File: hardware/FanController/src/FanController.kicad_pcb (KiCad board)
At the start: 2 copper layers, 54 x 12 mm, 12 parts, among them J1 MC 1,5/2, J2 Fan, J3 Fan, J4 Fan, J5 Fan, U1 12F1501, U2 MCP9701A

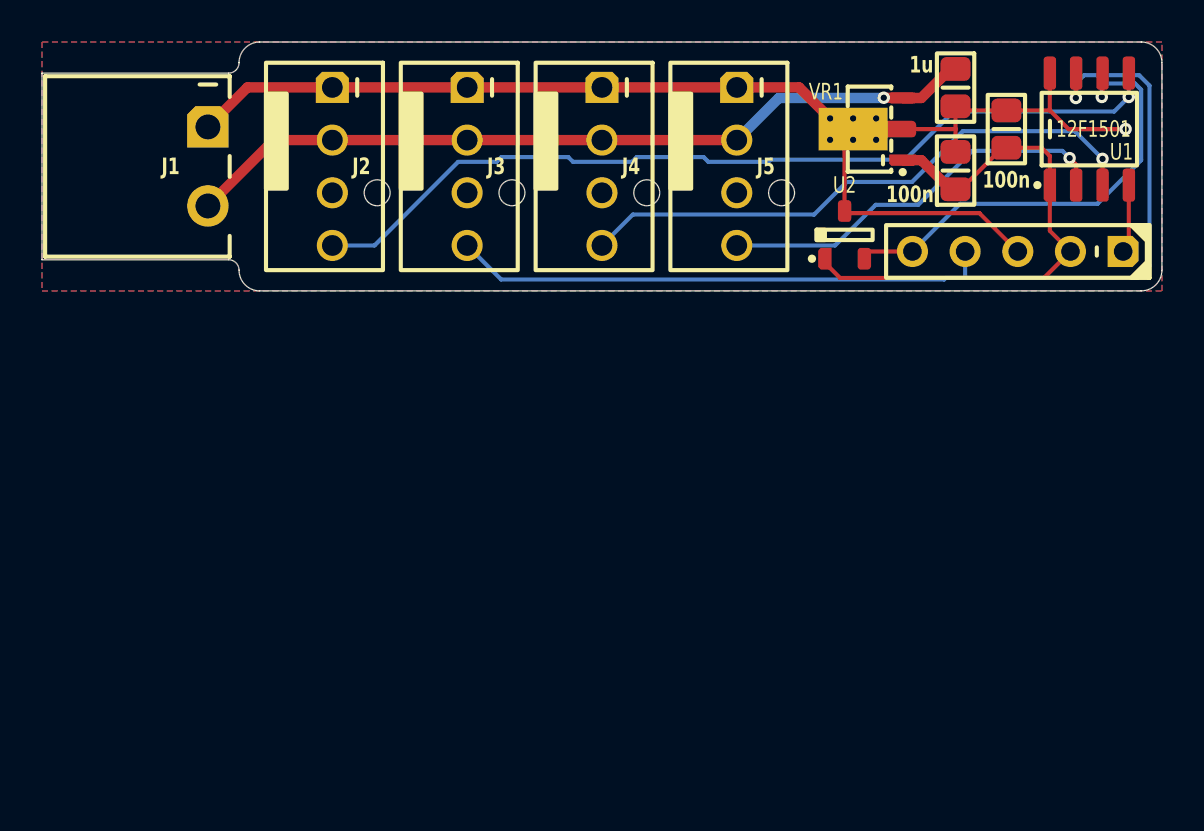
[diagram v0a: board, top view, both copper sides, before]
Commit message: Redesigned FanController board
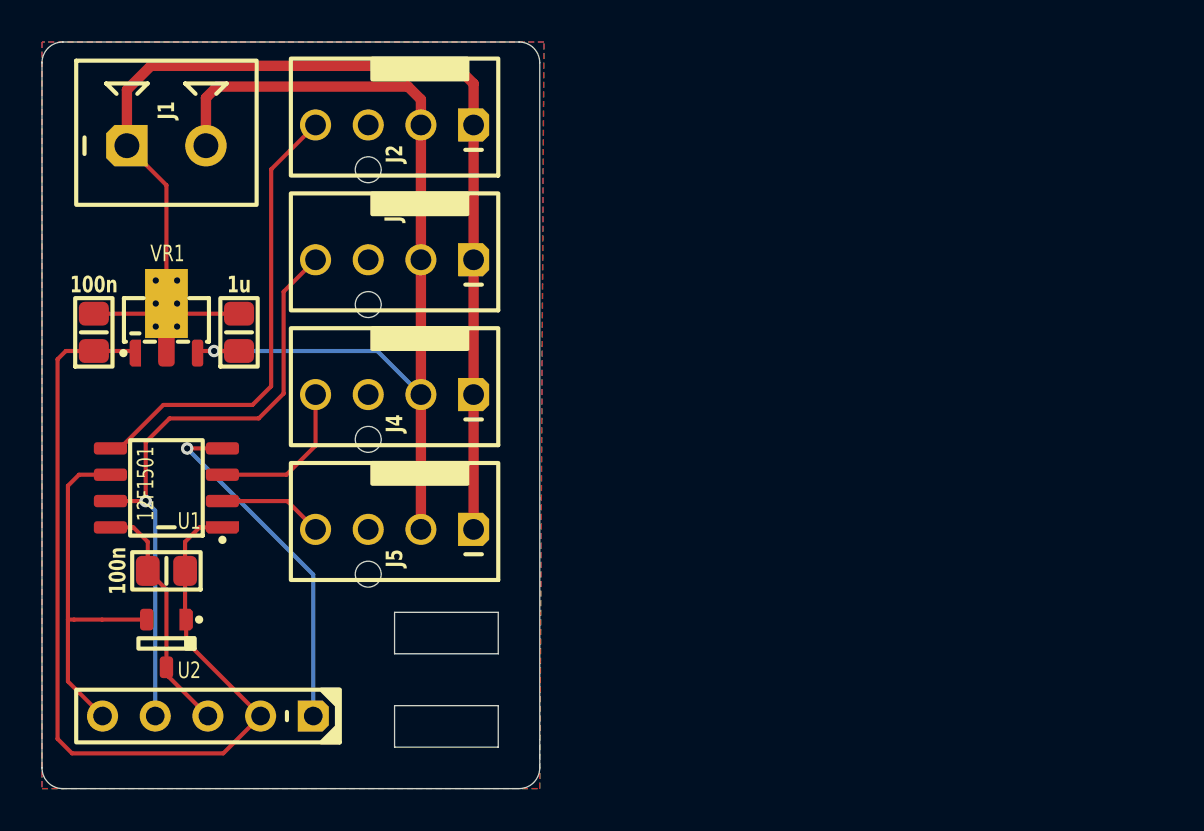
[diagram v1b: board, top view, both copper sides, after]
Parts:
- J1: footprint Medo64:J Phoenix MC (2w) -> Medo64:J Phoenix MCV (2w)
- moved U1 47.7 mm to (21.0, 36.5), turned to 180 degrees
- moved C1 45.8 mm to (21.0, 40.5), turned to 180 degrees
- moved ICSP 45.0 mm to (23.0, 47.5)
- moved C2 42.3 mm to (17.5, 29.0)
- moved U2 38.2 mm to (21.0, 44.0), turned to 180 degrees
- moved VR1 37.1 mm to (21.0, 30.0), turned to 0 degrees
- moved C3 36.5 mm to (24.5, 29.0), turned to 90 degrees
- moved J5 24.1 mm to (32.0, 38.5), turned to 180 degrees
- moved J4 14.9 mm to (32.0, 32.0), turned to 180 degrees
- moved J3 5.70 mm to (32.0, 25.5), turned to 180 degrees
- moved J2 3.61 mm to (32.0, 19.0), turned to 180 degrees
- moved J1 2.24 mm to (21.0, 20.0), turned to 0 degrees
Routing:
- net OUT_PWM1: track 42.9 -> 22.0 mm, vias 1 -> 0
- net OUT_PWM3: track 28.2 -> 7.53 mm, vias 1 -> 0
- net OUT_PWM2: track 49.7 -> 29.8 mm
- net +5V: track 25.7 -> 44.9 mm
- net OUT_PWM4: track 19.5 -> 5.06 mm, vias 1 -> 0
- net ICSP_VPP: track 2.93 -> 17.1 mm, vias 0 -> 1
- net +12V: track 38.5 -> 47.8 mm
- net ADC_TEMPERATURE: track 22.3 -> 17.9 mm, vias 1 -> 0
- net GND: track 69.3 -> 72.4 mm, vias 1 -> 0
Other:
- board size 54 x 12 mm -> 24 x 36 mm
